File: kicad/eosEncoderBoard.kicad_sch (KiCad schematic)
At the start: 0 parts

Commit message: schematic half done
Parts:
- added DP1: Display1, Connector_PinSocket_2.54mm:PinSocket_1x04_P2.54mm_Vertical, symbol Connector_Generic:Conn_01x04
- added DP2: Display2, Connector_PinSocket_2.54mm:PinSocket_1x04_P2.54mm_Vertical, symbol Connector_Generic:Conn_01x04
- added DP3: Display3, Connector_PinSocket_2.54mm:PinSocket_1x04_P2.54mm_Vertical, symbol Connector_Generic:Conn_01x04
- added DP4: Display4, Connector_PinSocket_2.54mm:PinSocket_1x04_P2.54mm_Vertical, symbol Connector_Generic:Conn_01x04
- added R1, R10, R11, R12, R13, R14, R15, R16, R17, R18, R19, R2, R3, R4, R5, R6, R7, R8, R9: 10k, symbol Device:R_Small
- added SW1, SW2, SW3, SW4: RotaryEncoder, Rotary_Encoder:RotaryEncoder_Alps_EC11E-Switch_Vertical_H20mm_MountingHoles, symbol Device:RotaryEncoder_Switch_MP
- added U1: Teensy3.2, Teensy:Teensy30_31_32_LC, symbol Teensy:Teensy3.2
- added U2: PCA9548APW, Package_SO:TSSOP-24_4.4x7.8mm_P0.65mm, symbol Interface_Expansion:PCA9548APW
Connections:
- new net +3.3V: DP1.3 (Pin_3), DP2.3 (Pin_3), DP3.3 (Pin_3), DP4.3 (Pin_3), R1.1, R10.1, R11.1, R12.1, R13.2, R14.2, R15.2, R16.2, R17.2, R18.2, R19.2, R2.1, R3.1, R4.1, R5.1, R6.1, R7.1, R8.1, R9.1, U2.24 (VCC)
- new net A1: R2.2, SW1.A
- new net A2: R4.2, SW2.A
- new net A3: R7.2, SW3.A
- new net A4: R8.2, SW4.A
- new net B1: R1.2, SW1.B
- new net B2: R3.2, SW2.B
- new net B3: R5.2, SW3.B
- new net B4: R6.2, SW4.B
- new net GND: DP1.4 (Pin_4), DP2.4 (Pin_4), DP3.4 (Pin_4), DP4.4 (Pin_4), SW1.C, SW1.S2, SW2.C, SW2.S2, SW3.C, SW3.S2, SW4.C, SW4.S2, U2.1 (A0), U2.12 (GND), U2.2 (A1), U2.21 (A2)
- new net RST: R19.1, U2.3 (~{RESET})
- new net SCL: R17.1, U2.22 (SCL)
- new net SCL1: DP1.2 (Pin_2), R9.2, U2.5 (SC0)
- new net SCL2: DP2.2 (Pin_2), R11.2, U2.7 (SC1)
- new net SCL3: DP3.2 (Pin_2), R13.1, U2.9 (SC2)
- new net SCL4: DP4.2 (Pin_2), R15.1, U2.11 (SC3)
- new net SDA: R18.1, U2.23 (SDA)
- new net SDA1: DP1.1 (Pin_1), R10.2, U2.4 (SD0)
- new net SDA2: DP2.1 (Pin_1), R12.2, U2.6 (SD1)
- new net SDA3: DP3.1 (Pin_1), R14.1, U2.8 (SD2)
- new net SDA4: DP4.1 (Pin_1), R16.1, U2.10 (SD3)
- new net SW1: SW1.S1
- new net SW2: SW2.S1
- new net SW3: SW3.S1
- new net SW4: SW4.S1
- no-connect marks 0 -> 12
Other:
- note added: "Display Headers"
- note added: "Encoders"
- note added: "I2C Mux"

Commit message: schematic basically done
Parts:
- removed U1: Teensy3.2, Teensy:Teensy30_31_32_LC, symbol Teensy:Teensy3.2
- added C1, C2, C3, C4, C8: 0.1u, symbol Device:C_Small
- added C10: 22u, symbol Device:C_Small
- added C5: 1u, symbol Device:C_Small
- added C6: 10u, symbol Device:C_Small
- added C7: 10n, symbol Device:C_Small
- added C9: 4.7u, symbol Device:C_Small
- added D1: INTENS, symbol Device:LED
- added D2: FORM, symbol Device:LED
- added D3: FOCUS, symbol Device:LED
- added D4: IMAGE, symbol Device:LED
- added D5: COLOR, symbol Device:LED
- added D6: SHUTTER, symbol Device:LED
- added D7: LED, symbol Device:LED
- added J1: USB_C_Receptacle_USB2.0_16P, Connector_USB:USB_C_Receptacle_GCT_USB4105-xx-A_16P_TopMnt_Horizontal, symbol Connector:USB_C_Receptacle_USB2.0_16P
- added J2: DEBUG, Connector_PinSocket_2.54mm:PinSocket_1x06_P2.54mm_Vertical, symbol Connector_Generic:Conn_01x06
- added J3: EXTRA, Connector_PinSocket_2.54mm:PinSocket_1x06_P2.54mm_Vertical, symbol Connector_Generic:Conn_01x06
- added L1: 1.0u, symbol Device:L_Small
- added R20, R21, R22, R23, R24, R25: 150, symbol Device:R_Small
- added R26, R27: 5.1k, symbol Device:R_Small
- added R28: 10k, symbol Device:R_Small
- added R29: 453k, symbol Device:R_Small
- added R30: 100k, symbol Device:R_Small
- added R31: 270, symbol Device:R_Small
- added SW10: SHUTTER, Button_Switch_Keyboard:SW_Cherry_MX_1.00u_PCB, symbol Switch:SW_Push
- added SW11: SW_Push, symbol Switch:SW_Push
- added SW5: INTENS, Button_Switch_Keyboard:SW_Cherry_MX_1.00u_PCB, symbol Switch:SW_Push
- added SW6: FORM, Button_Switch_Keyboard:SW_Cherry_MX_1.00u_PCB, symbol Switch:SW_Push
- added SW7: FOCUS, Button_Switch_Keyboard:SW_Cherry_MX_1.00u_PCB, symbol Switch:SW_Push
- added SW8: IMAGE, Button_Switch_Keyboard:SW_Cherry_MX_1.00u_PCB, symbol Switch:SW_Push
- added SW9: COLOR, Button_Switch_Keyboard:SW_Cherry_MX_1.00u_PCB, symbol Switch:SW_Push
- added U1: STM32L072CZTx, Package_QFP:LQFP-48_7x7mm_P0.5mm, symbol MCU_ST_STM32L0:STM32L072CZTx
- added U3: TPS62A01DRL, Package_TO_SOT_SMD:SOT-563, symbol Regulator_Switching:TPS62A01DRL
- added Y1: OSC16M-3.3I/S3T, Oscillator:Oscillator_SMD_Abracon_ASE-4Pin_3.2x2.5mm, symbol Oscillator:SG-8002CE
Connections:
- net +3.3V: now also C1.1, C10.1, C2.1, C3.1, C4.1, C5.1, C6.1, C7.1, D7.2 (A), J2.1 (Pin_1), J3.1 (Pin_1), L1.2, R29.1, U1.1 (VDD), U1.24 (VDD), U1.36 (VDD_USB), U1.48 (VDD), U1.9 (VDDA), Y1.4 (Vcc)
- net A1: now also U1.16 (PA6)
- net A2: now also U1.10 (PA0)
- net A3: now also U1.12 (PA2)
- net A4: now also U1.40 (PB4)
- net B1: now also U1.17 (PA7)
- net B2: now also U1.11 (PA1)
- net B3: now also U1.13 (PA3)
- net B4: now also U1.41 (PB5)
- net GND: now also C1.2, C10.2, C2.2, C3.2, C4.2, C5.2, C6.2, C7.2, C8.2, C9.2, J1.A1 (GND), J1.A12 (GND), J1.B1 (GND), J1.B12 (GND), J2.6 (Pin_6), J3.6 (Pin_6), R20.2, R21.2, R22.2, R23.2, R24.2, R25.2, R26.1, R27.2, R28.2, R30.2, R31.2, SW10.2, SW11.1, SW5.2, SW6.2, SW7.2, SW8.2, SW9.2, U1.23 (VSS), U1.35 (VSS), U1.47 (VSS), U1.8 (VSSA), U3.1 (GND), Y1.2 (GND)
- net RST: now also U1.29 (PA8)
- net SCL: now also U1.30 (PA9)
- net SDA: now also U1.31 (PA10)
- net SW1: now also U1.14 (PA4)
- net SW2: now also U1.15 (PA5)
- net SW3: now also U1.18 (PB0)
- net SW4: now also U1.19 (PB1)
- new net: D2.1 (K), R21.1
- new net: D7.1 (K), R31.1
- new net: L1.1, U3.2 (SW)
- new net: R29.2, R30.1, U3.5 (FB)
- new net: J1.A5 (CC1), R26.2
- new net: J1.B5 (CC2), R27.1
- new net: D3.1 (K), R22.1
- new net: D5.1 (K), R24.1
- new net: D6.1 (K), R25.1
- new net: D1.1 (K), R20.1
- new net: D4.1 (K), R23.1
- new net +5V: C9.1, J1.A4 (VBUS), J1.A9 (VBUS), J1.B4 (VBUS), J1.B9 (VBUS), U3.3 (VIN), U3.4 (EN)
- new net BOOT0: J2.5 (Pin_5), R28.1, U1.44 (BOOT0)
- new net BTN_COLOR: SW9.1, U1.42 (PB6)
- new net BTN_FOCUS: SW7.1, U1.39 (PB3)
- new net BTN_FORM: SW6.1, U1.46 (PB9)
- new net BTN_IMAGE: SW8.1, U1.45 (PB8)
- new net BTN_INTENS: SW5.1, U1.20 (PB2)
- new net BTN_SHUTTER: SW10.1, U1.43 (PB7)
- new net CLK: U1.5 (PH0), Y1.3 (OUT)
- new net D+: J1.A6 (D+), J1.B6 (D+), U1.33 (PA12)
- new net D-: J1.A7 (D-), J1.B7 (D-), U1.32 (PA11)
- new net EXTRA1: J3.2 (Pin_2), U1.2 (PC13)
- new net EXTRA2: J3.3 (Pin_3), U1.3 (PC14)
- new net EXTRA3: J3.4 (Pin_4), U1.4 (PC15)
- new net EXTRA4: J3.5 (Pin_5), U1.38 (PA15)
- new net LED_COLOR: D5.2 (A), U1.25 (PB12)
- new net LED_FOCUS: D3.2 (A), U1.22 (PB11)
- new net LED_FORM: D2.2 (A), U1.28 (PB15)
- new net LED_IMAGE: D4.2 (A), U1.27 (PB14)
- new net LED_INTENS: D1.2 (A), U1.21 (PB10)
- new net LED_SHUTTER: D6.2 (A), U1.26 (PB13)
- new net SWCLK: J2.3 (Pin_3), U1.37 (PA14)
- new net SWDIO: J2.2 (Pin_2), U1.34 (PA13)
- new net ~{RST}: C8.1, J2.4 (Pin_4), SW11.2, U1.7 (NRST)
- no-connect marks 12 -> 17
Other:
- note added: "16MHz Clock"
- note added: "3.3V Regulator"
- note added: "Debug Header"
- note added: "Decoupling Caps"
- note added: "Extra Header"
- note added: "Microcontroller"
- note added: "Parameter Buttons"
- note added: "Place 1u near VDDA Place 1x0.1u near each VDD+VDDA"
- note added: "Reset Button"
- note added: "Todo: Check Footprints for all items Build digikey list PCB layout"
- note added: "USB Connector"
- moved on the sheet: DP1, DP2, DP3, DP4, R10, R11, R12, R13, R14, R15, R16, R17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

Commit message: schematic done and code todo updated
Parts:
- removed U2: PCA9548APW, Package_SO:TSSOP-24_4.4x7.8mm_P0.65mm, symbol Interface_Expansion:PCA9548APW
- added R32: 150, Resistor_SMD:R_0603_1608Metric, symbol Device:R_Small
- added U2: PCA9548ADB, Package_SO:SSOP-24_5.3x8.2mm_P0.65mm, symbol Interface_Expansion:PCA9548ADB
- C1, C10, C2, C3, C4, C5, C6, C7, C8, C9: footprint (none) -> Capacitor_SMD:C_0603_1608Metric
- D1, D2, D3, D4, D5, D6, D7: footprint (none) -> LED_SMD:LED_0603_1608Metric
- L1: footprint (none) -> Inductor_SMD:L_1008_2520Metric
- R1, R10, R11, R12, R13, R14, R15, R16, R17, R18, R19, R2, R20, R21, R22, R23, R24, R25, R26, R27, R28, R29, R3, R30, R4, R5, R6, R7, R8, R9: footprint (none) -> Resistor_SMD:R_0603_1608Metric
- R31: value 270 -> 150; footprint (none) -> Resistor_SMD:R_0603_1608Metric
- SW1: footprint Rotary_Encoder:RotaryEncoder_Alps_EC11E-Switch_Vertical_H20mm_MountingHoles -> Rotary_Encoder:RotaryEncoder_Alps_EC11E-Switch_Vertical_H20mm
- SW11: footprint (none) -> Button_Switch_SMD:SW_Push_1P1T_XKB_TS-1187A
- U1: value STM32L072CZTx -> STM32L072CZT6TR
- U3: value TPS62A01DRL -> TPS62A01DRLR
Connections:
- net +3.3V: now also U2.24 (VCC)
- net GND: now also R32.2, U2.1 (A0), U2.12 (GND), U2.2 (A1), U2.21 (A2); no longer R31.2
- net RST: now also U2.3 (~{RESET})
- net SCL: now also U2.22 (SCL)
- net SCL1: now also U2.5 (SC0)
- net SCL2: now also U2.7 (SC1)
- net SCL3: now also U2.9 (SC2)
- net SCL4: now also U2.11 (SC3)
- net SDA: now also U2.23 (SDA)
- net SDA1: now also U2.4 (SD0)
- net SDA2: now also U2.6 (SD1)
- net SDA3: now also U2.8 (SD2)
- net SDA4: now also U2.10 (SD3)
- new net: R31.2, R32.1
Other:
- note removed: "Todo: Check Footprints for all items Build digikey list PCB layout"

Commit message: pcb started kinda
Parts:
- SW2, SW3, SW4: footprint Rotary_Encoder:RotaryEncoder_Alps_EC11E-Switch_Vertical_H20mm_MountingHoles -> Rotary_Encoder:RotaryEncoder_Alps_EC11E-Switch_Vertical_H20mm
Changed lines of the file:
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@@
 			)
 		)
-		(property "Footprint" "Rotary_Encoder:RotaryEncoder_Alps_EC11E-Switch_Vertical_H20mm_MountingHoles"
+		(property "Footprint" "Rotary_Encoder:RotaryEncoder_Alps_EC11E-Switch_Vertical_H20mm"
 			(at 261.62 89.916 0)
 			(hide yes)
@@
 			)
 		)
-		(property "Footprint" "Rotary_Encoder:RotaryEncoder_Alps_EC11E-Switch_Vertical_H20mm_MountingHoles"
+		(property "Footprint" "Rotary_Encoder:RotaryEncoder_Alps_EC11E-Switch_Vertical_H20mm"
 			(at 261.62 69.596 0)
 			(hide yes)
@@
 			)
 		)
-		(property "Footprint" "Rotary_Encoder:RotaryEncoder_Alps_EC11E-Switch_Vertical_H20mm_MountingHoles"
+		(property "Footprint" "Rotary_Encoder:RotaryEncoder_Alps_EC11E-Switch_Vertical_H20mm"
 			(at 261.62 49.276 0)
 			(hide yes)

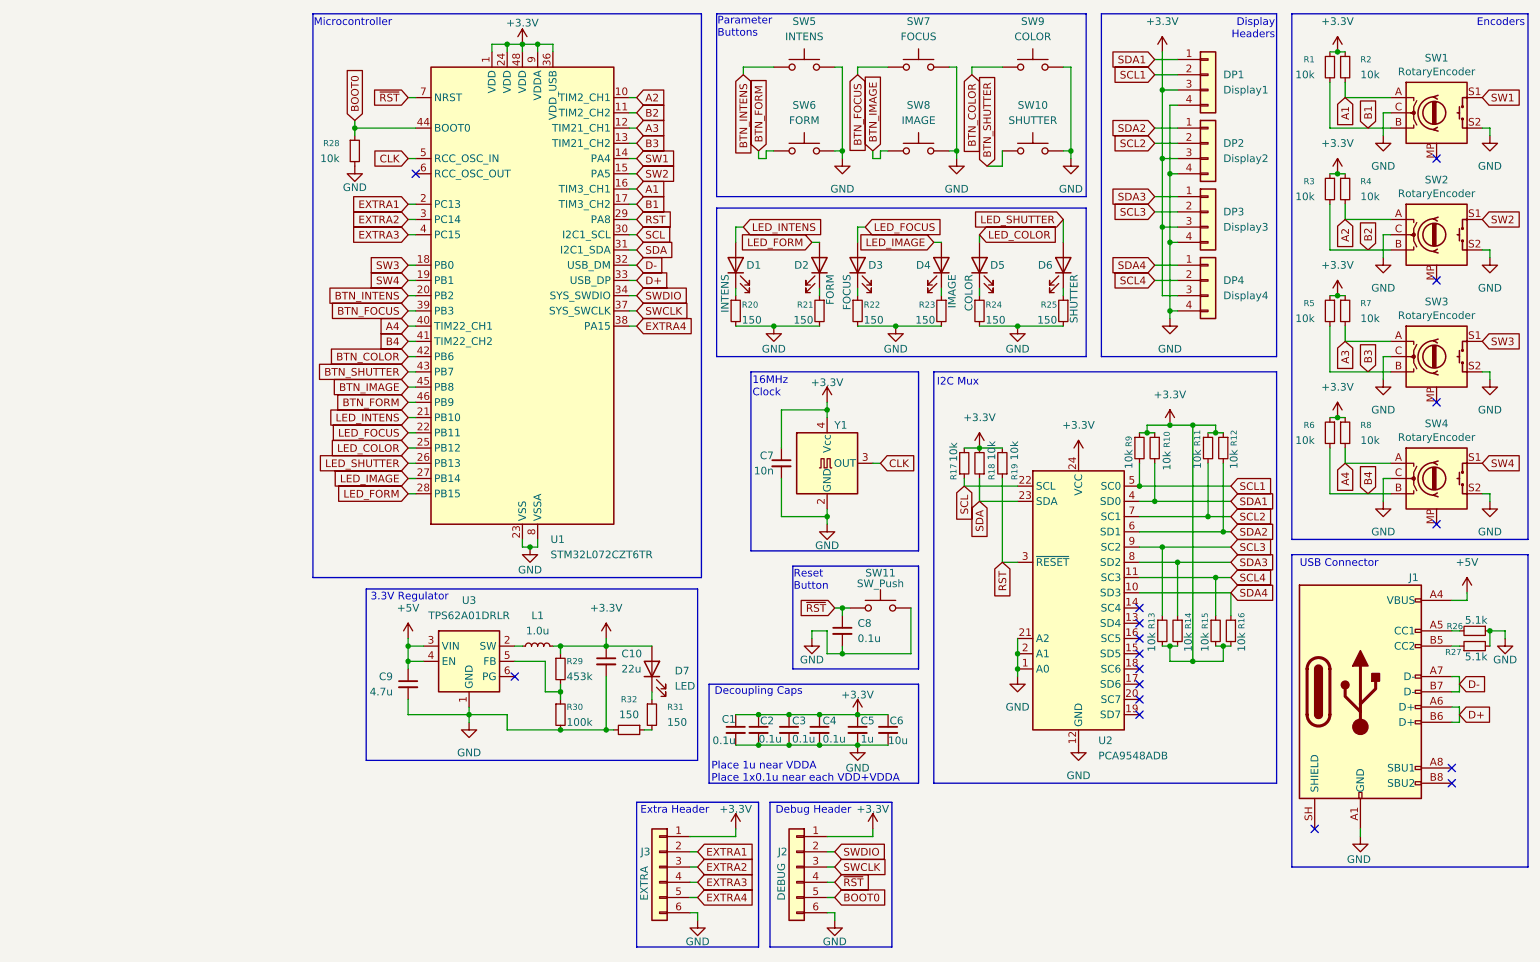
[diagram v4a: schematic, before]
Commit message: pcb layout done, still need to handle silkscreen and add mounting holes and such
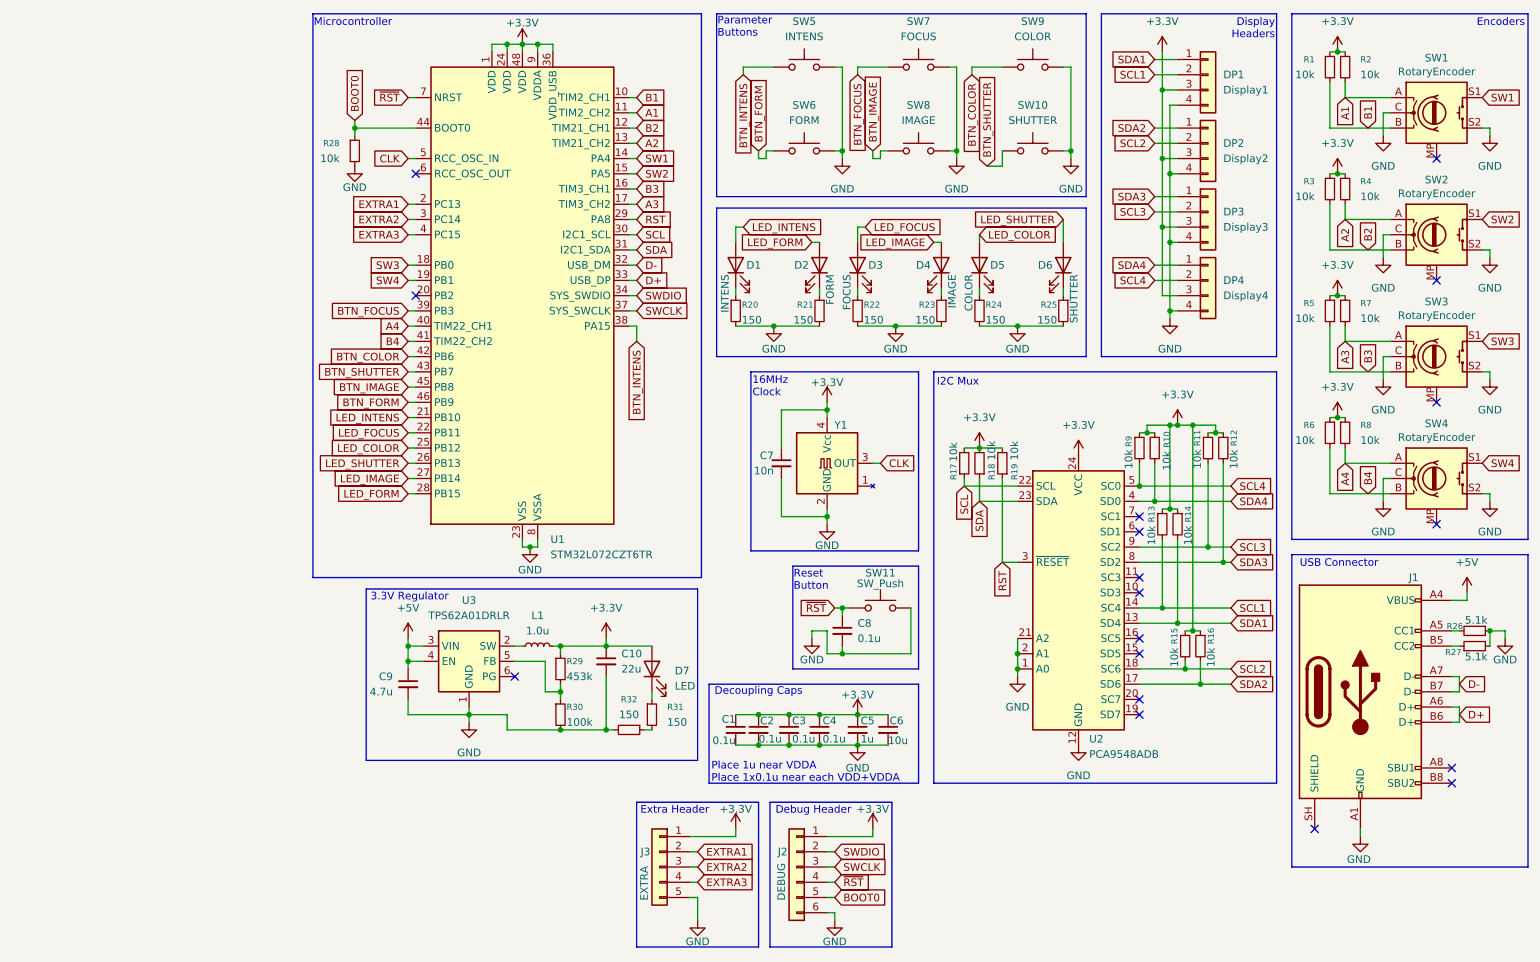
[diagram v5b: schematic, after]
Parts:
- J3: footprint Connector_PinSocket_2.54mm:PinSocket_1x06_P2.54mm_Vertical -> Connector_PinSocket_2.54mm:PinSocket_1x05_P2.54mm_Vertical; symbol Connector_Generic:Conn_01x06 -> Connector_Generic:Conn_01x05
- SW10, SW5, SW6, SW7, SW8, SW9: footprint Button_Switch_Keyboard:SW_Cherry_MX_1.00u_PCB -> SwitchLED:SW_Cherry_MX_1.00u_PCB_LED0603
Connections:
- net +3.3V: now also R13.1, R14.1, R15.1, R16.1; no longer R13.2, R14.2, R15.2, R16.2
- net A1: now also U1.11 (PA1); no longer U1.16 (PA6)
- net A2: now also U1.13 (PA3); no longer U1.10 (PA0)
- net A3: now also U1.17 (PA7); no longer U1.12 (PA2)
- net B1: now also U1.10 (PA0); no longer U1.17 (PA7)
- net B2: now also U1.12 (PA2); no longer U1.11 (PA1)
- net B3: now also U1.16 (PA6); no longer U1.13 (PA3)
- net BTN_INTENS: now also U1.38 (PA15); no longer U1.20 (PB2)
- net GND: now also J3.5 (Pin_5); no longer J3.6 (Pin_6)
- net SCL1: now also R13.2, U2.14 (SC4); no longer R9.2, U2.5 (SC0)
- net SCL2: now also R15.2, U2.18 (SC6); no longer R11.2, U2.7 (SC1)
- net SCL3: now also R11.2; no longer R13.1
- net SCL4: now also R9.2, U2.5 (SC0); no longer R15.1, U2.11 (SC3)
- net SDA1: now also R14.2, U2.13 (SD4); no longer R10.2, U2.4 (SD0)
- net SDA2: now also R16.2, U2.17 (SD6); no longer R12.2, U2.6 (SD1)
- net SDA3: now also R12.2; no longer R14.1
- net SDA4: now also R10.2, U2.4 (SD0); no longer R16.1, U2.10 (SD3)
- removed net EXTRA4: J3.5 (Pin_5), U1.38 (PA15)
- no-connect marks 17 -> 18

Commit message: pcb done other than silkscreen
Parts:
- DP1, DP2, DP3, DP4: footprint Connector_PinSocket_2.54mm:PinSocket_1x04_P2.54mm_Vertical -> Connector_PinHeader_2.54mm:PinHeader_1x04_P2.54mm_Vertical
- SW10, SW5, SW6, SW7, SW8, SW9: footprint SwitchLED:SW_Cherry_MX_1.00u_PCB_LED0603 -> SwitchLED:SW_Cherry_MX_PCB_1.00u_LED0603
- renumbered R29 to RFB1, R30 to RFB2, R26 to RUSB1, R27 to RUSB2
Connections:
- net +3.3V: now also J2.6 (Pin_6), J3.5 (Pin_5); no longer J2.1 (Pin_1), J3.1 (Pin_1)
- net BOOT0: now also J2.2 (Pin_2); no longer J2.5 (Pin_5)
- net EXTRA1: now also J3.4 (Pin_4); no longer J3.2 (Pin_2)
- net EXTRA3: now also J3.2 (Pin_2); no longer J3.4 (Pin_4)
- net GND: now also J2.1 (Pin_1), J3.1 (Pin_1); no longer J2.6 (Pin_6), J3.5 (Pin_5)
- net SWCLK: now also J2.4 (Pin_4); no longer J2.3 (Pin_3)
- net SWDIO: now also J2.5 (Pin_5); no longer J2.2 (Pin_2)
- net ~{RST}: now also J2.3 (Pin_3); no longer J2.4 (Pin_4)
